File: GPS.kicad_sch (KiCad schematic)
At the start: 10 parts, among them J3 Conn_Coaxial, U2 ATGM336H, U8 AT24C32A

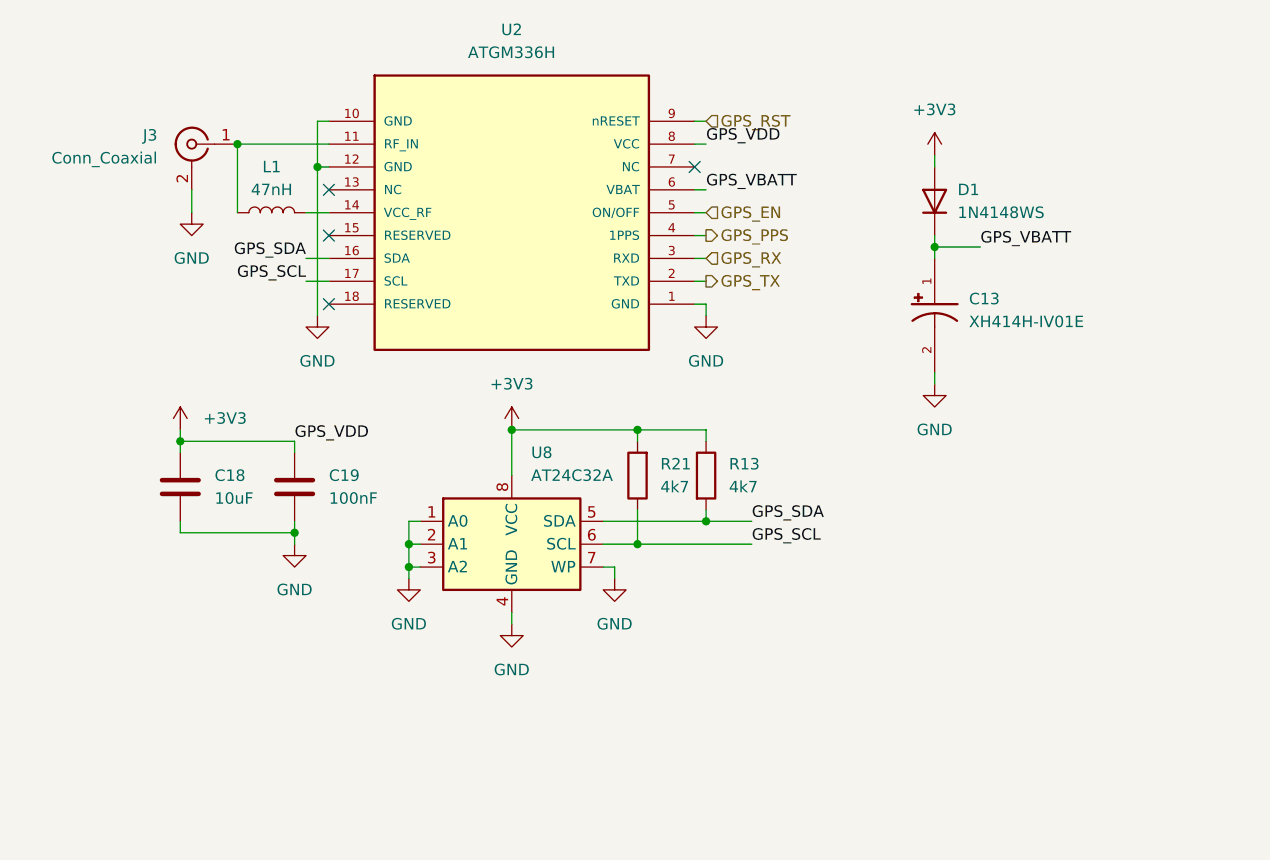
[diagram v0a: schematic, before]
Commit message: Round board corners, re-annotate test points, rewrite README for GitHub
Board: 1.0 mm radius corners; outline now 71.00 x 46.00 mm.
Schematic: test points re-annotated to signal names (SDA1, SLC1,
CSN1, CLK1, MOSI1, MISO1, VS1, G1, G2, IO7, IO15, IO47, RST1, BOOT1).

README rewritten as a GitHub landing page: explains what the board is
for, adds Mermaid system-architecture and power-path diagrams, a
verified pin map traced from the netlist, board specs, and fab
instructions. Drops the ERC/DRC status and issue-tracking sections.

Co-Authored-By: Claude Opus 5 <noreply@anthropic.com>
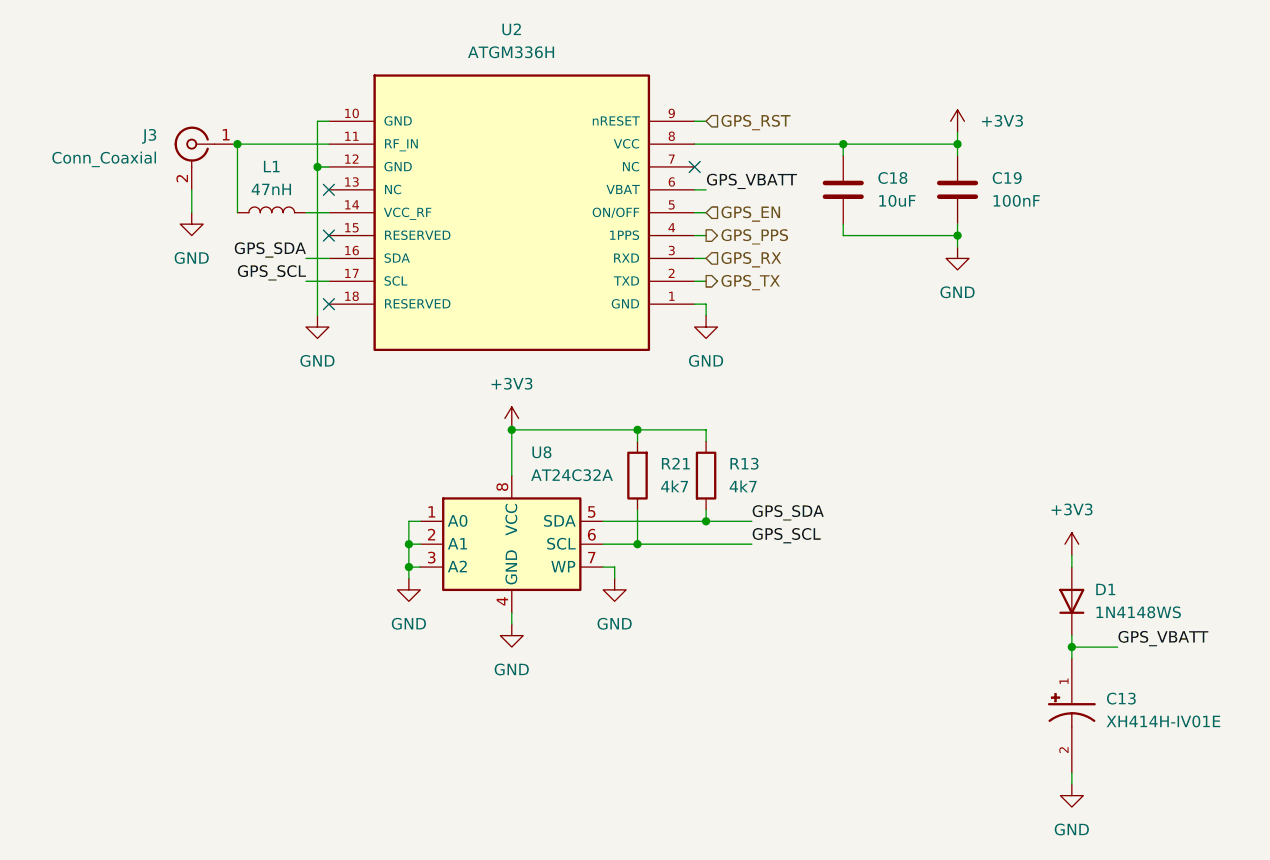
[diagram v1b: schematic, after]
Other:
- moved on the sheet: C13, D1
